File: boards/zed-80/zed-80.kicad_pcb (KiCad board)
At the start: 2 copper layers, 102.5 x 70 mm, 34 parts, among them J401 TYPE-C-31-M-12, SW201 SW_Push, U201 GD74LS04, U202 Z84C0010PEC, U301 TT74LS32BI, U302 AT28C256-15PU, U303 HM628128BLP-10, U401 CH340C, U402 MC68B50P, Y201 7.3728 MHz

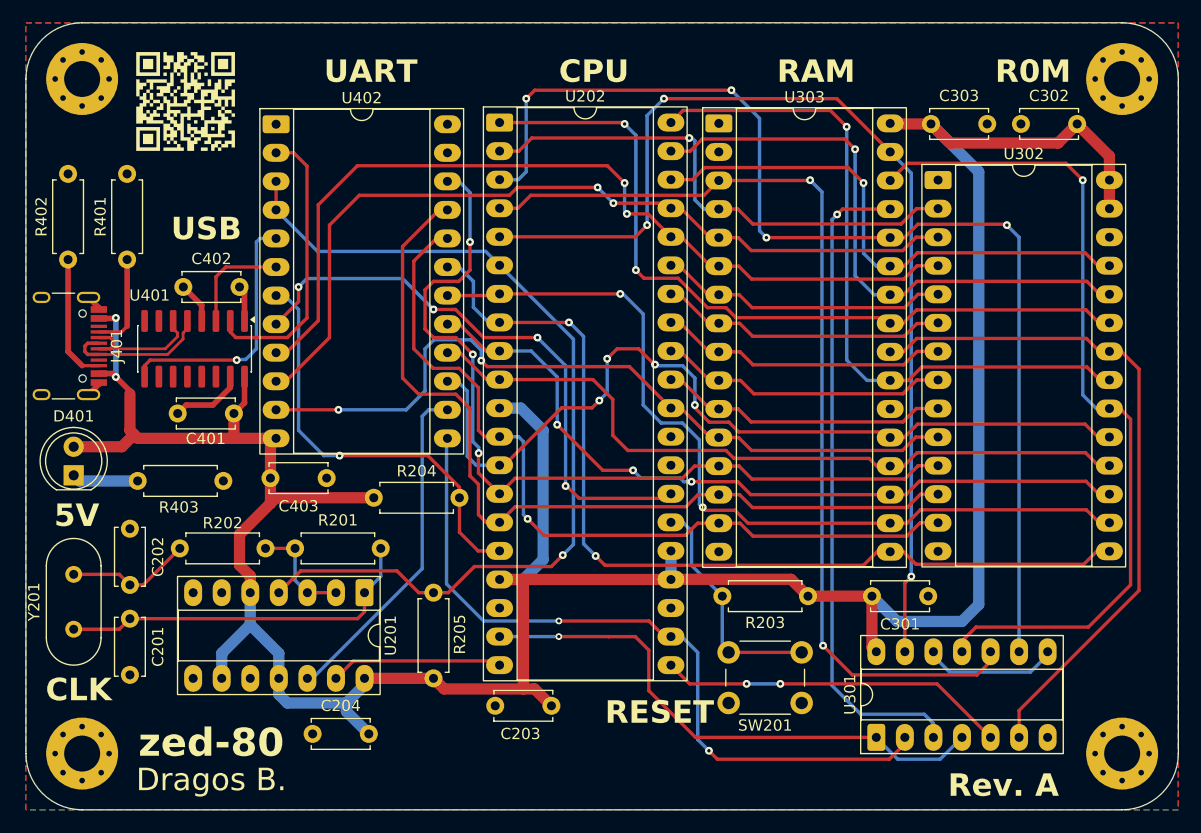
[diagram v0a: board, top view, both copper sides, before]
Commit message: Shortened main board
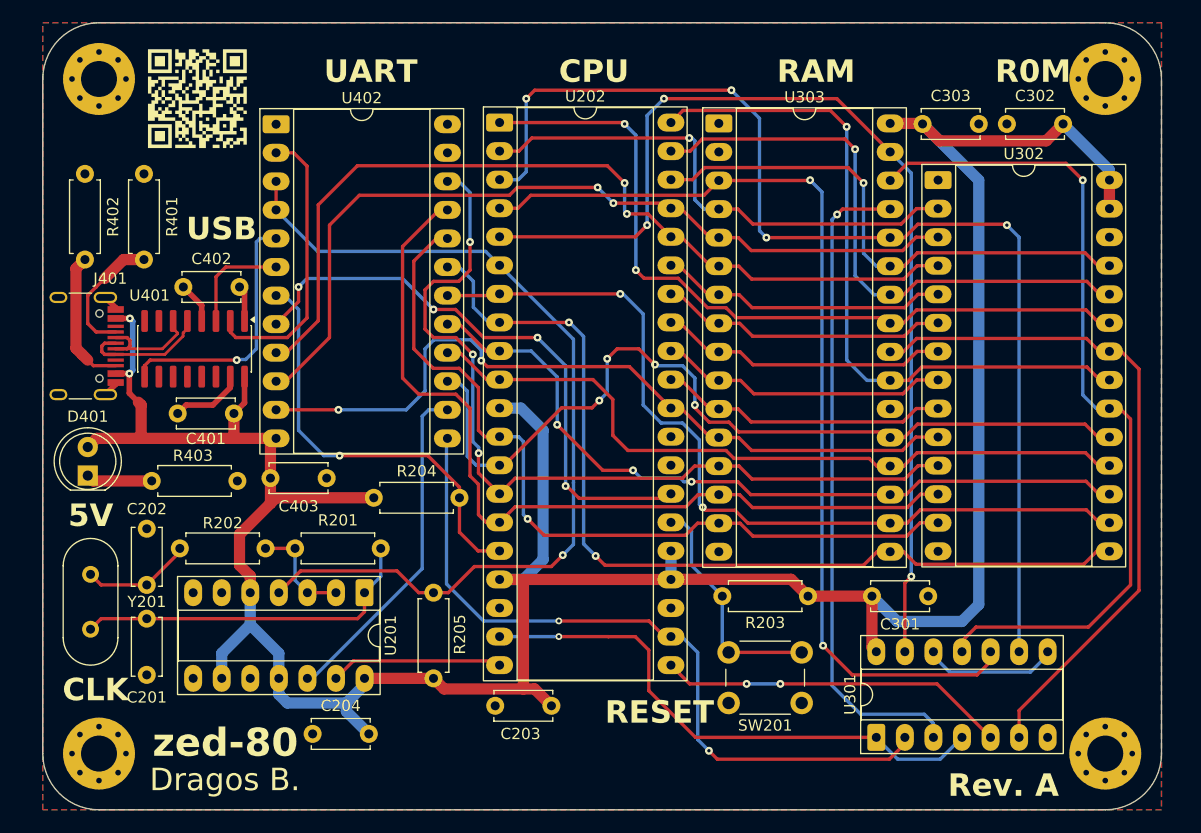
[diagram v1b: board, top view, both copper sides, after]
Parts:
- moved C201 1.50 mm to (90.8, 95.5)
- moved C202 1.50 mm to (90.8, 92.5)
- moved J401 1.50 mm to (83.9, 71.2)
- moved MH101 1.50 mm to (86.5, 47.5)
- moved MH102 1.50 mm to (176.0, 47.5)
- moved MH103 1.50 mm to (86.5, 107.5)
- moved MH104 1.50 mm to (176.0, 107.5)
- moved R401 1.50 mm to (90.5, 63.6)
- moved R402 1.50 mm to (85.2, 63.6)
- moved Y201 1.50 mm to (85.8, 96.4)
- moved D401 1.25 mm to (85.5, 82.8)
- moved C302 1.25 mm to (167.2, 51.5)
- moved R403 1.25 mm to (91.2, 83.2)
- moved G*** 1.08 mm to (95.2, 49.2)
- moved C303 0.75 mm to (164.8, 51.5)
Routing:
- net Net-(J401-CC1): track 8.66 -> 11.6 mm
- net VBUS: track 263.5 -> 261.0 mm
- net Net-(C201-Pad1): track 32.7 -> 31.2 mm
- net Net-(C202-Pad1): track 11.2 -> 9.86 mm
- net /USB-to-UART/D+: track 12.3 -> 11.4 mm
- net /USB-to-UART/D-: track 11.6 -> 10.6 mm
- net Net-(J401-CC2): track 11.4 -> 12.4 mm
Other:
- board size 102.5 x 70 mm -> 99.5 x 70 mm

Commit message: Cleanup main board
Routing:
- net /USB-to-UART/D-: track 10.6 -> 9.91 mm
- net /USB-to-UART/D+: track 11.4 -> 10.7 mm
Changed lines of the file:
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@@
-	)
-	(segment
-		(start 93.69 89.56)
-		(end 93.69 89.25)
-		(width 0.3)
-		(layer "F.Cu")
-		(net 3)
 	)
 	(segment
@@
 	)
 	(segment
-		(start 85.5 80.235)
-		(end 85.515 80.235)
-		(width 1)
-		(layer "F.Cu")
-		(net 4)
-	)
-	(segment
 		(start 89.25 68.8)
 		(end 87.985 68.8)
@@
 	)
 	(segment
-		(start 159.7 51.45)
-		(end 159.75 51.5)
-		(width 1)
-		(layer "F.Cu")
-		(net 4)
-	)
-	(segment
 		(start 125.24 101.75)
 		(end 124.25 101.75)
@@
 	(segment
 		(start 86.285 79.465)
-		(end 89.75 79.465)
-		(width 1)
-		(layer "F.Cu")
-		(net 4)
-	)
-	(segment
-		(start 89.75 79.465)
 		(end 90.25 79.465)
 		(width 1)
@@
 	)
 	(segment
-		(start 94.365 69.025)
-		(end 94.365 69.7)
-		(width 0.25)
-		(layer "F.Cu")
-		(net 7)
-	)
-	(segment
 		(start 92.353554 72)
 		(end 87.985 72)
@@
 	)
 	(segment
-		(start 93.095 69.025)
-		(end 93.095 69.7)
-		(width 0.25)
-		(layer "F.Cu")
-		(net 8)
-	)
-	(segment
 		(start 89 70.5)
 		(end 89.25 70.75)
@@
 	(segment
 		(start 84.450001 71.450001)
-		(end 85 72)
-		(width 1)
-		(layer "F.Cu")
-		(net 11)
-	)
-	(segment
-		(start 85 72)
 		(end 85.5 72.5)
 		(width 1)
@@
 	)
 	(segment
-		(start 85.5 66.75)
-		(end 85.5 66.746504)
-		(width 0.3)
-		(layer "F.Cu")
-		(net 12)
-	)
-	(segment
 		(start 88.69 63.56)
 		(end 87 65.25)
@@
 	(segment
 		(start 85.5 69.25)
-		(end 85.5 66.75)
-		(width 0.3)
-		(layer "F.Cu")
+		(end 85.5 66.746504)
+		(width 0.3)
+		(layer "F.Cu")
